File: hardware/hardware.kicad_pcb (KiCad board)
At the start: 2 copper layers, 41 parts, among them J2 Conn_01x03, U1 CH32M007G8R6

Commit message: add shunt A- + led + ntc
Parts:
- added Q10: AOD514, AOD514:TRANS_AOD514, F.Cu at (88.4, 31.7)
- added Q11: AOD514, AOD514:TRANS_AOD514, F.Cu at (97.2, 31.7)
- added Q12: AOD514, AOD514:TRANS_AOD514, F.Cu at (106.1, 31.7)
- added Q7: AOD514, AOD514:TRANS_AOD514, F.Cu at (61.8, 31.7)
- added Q8: AOD514, AOD514:TRANS_AOD514, F.Cu at (70.6, 31.7)
- added Q9: AOD514, AOD514:TRANS_AOD514, F.Cu at (79.5, 31.7)
- moved C11 13.8 mm to (116.0, 50.3)

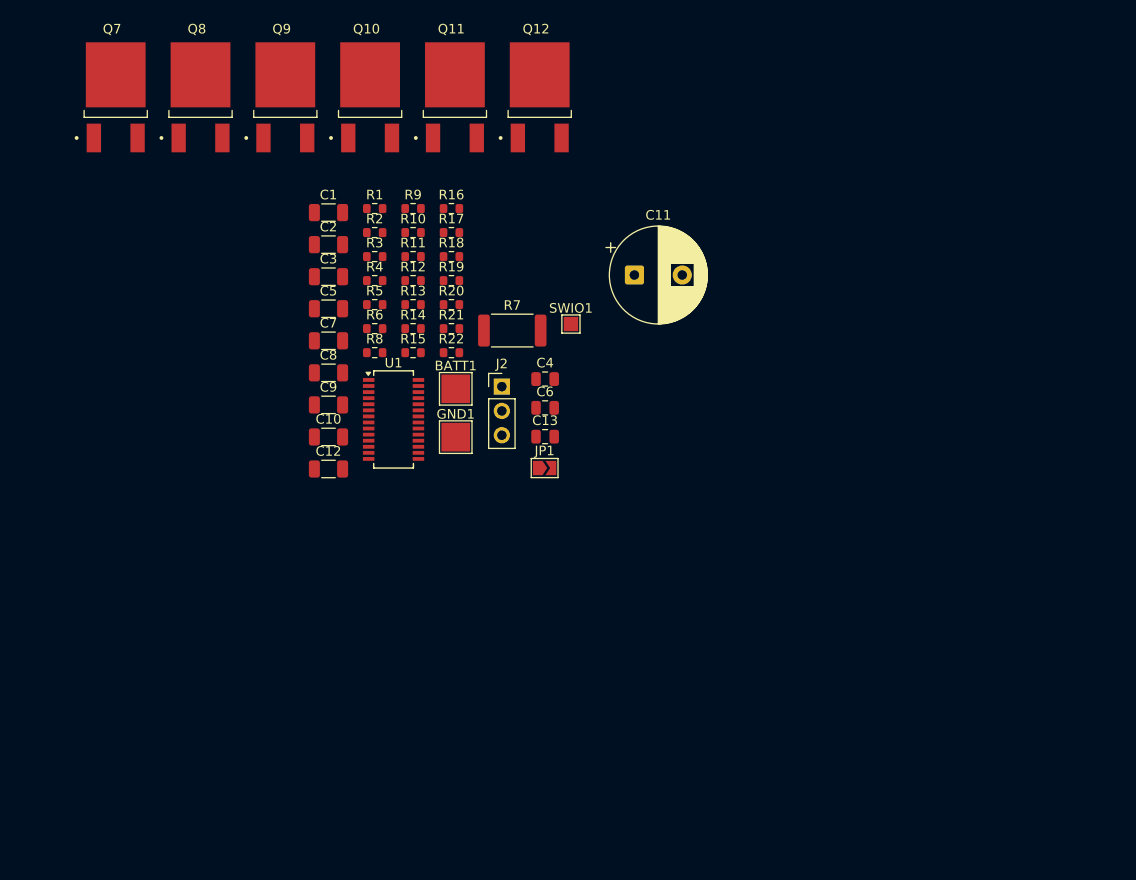
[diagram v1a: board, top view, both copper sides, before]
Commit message: first pcb position
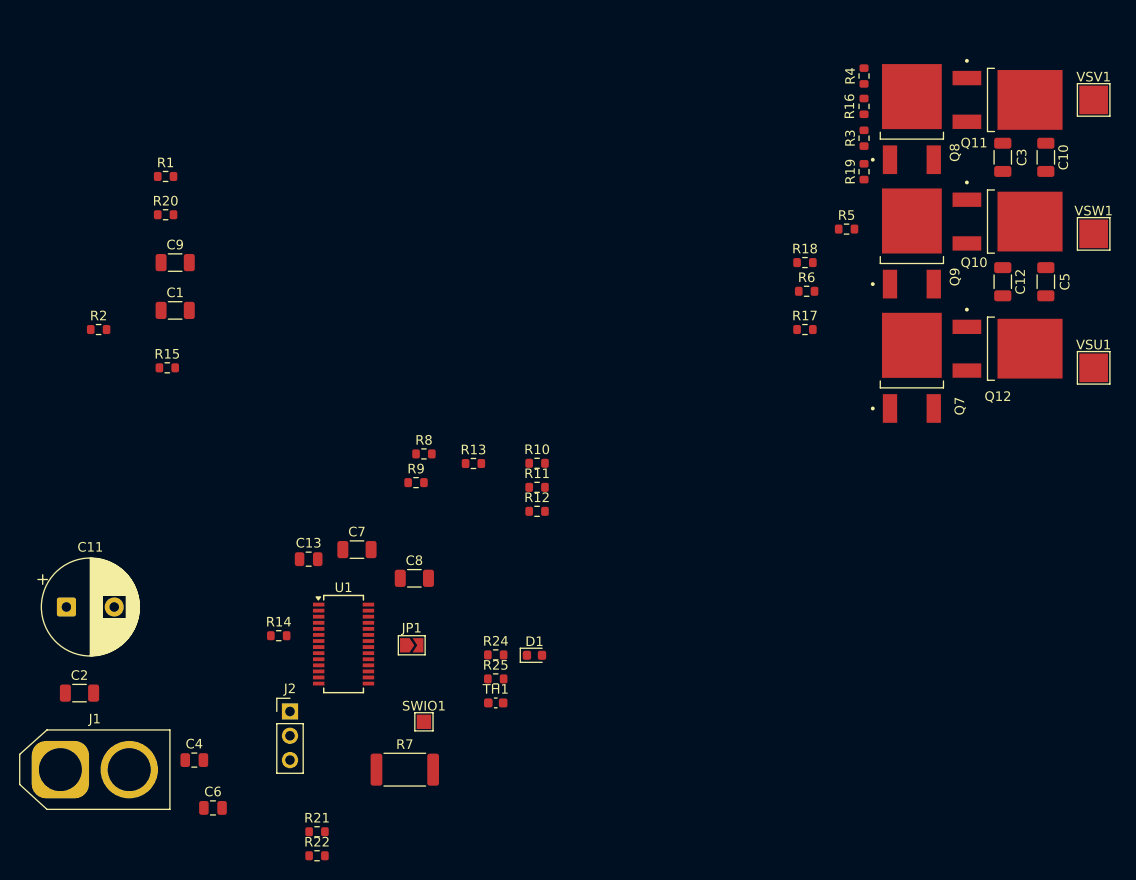
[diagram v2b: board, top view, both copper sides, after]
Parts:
- removed BATT1, GND1: TestPoint_Alt, TestPoint:TestPoint_Pad_3.0x3.0mm
- added D1: BLUE, LED_SMD:LED_0603_1608Metric, F.Cu at (105.6, 90.0)
- added J1: AMASS, Connector_AMASS:AMASS_XT60-F_1x02_P7.20mm_Vertical, F.Cu at (56.0, 102.0)
- added R24: 10k, Resistor_SMD:R_0603_1608Metric, F.Cu at (101.5, 90.0)
- added R25: 1.1k, Resistor_SMD:R_0603_1608Metric, F.Cu at (101.5, 92.5)
- added TH1: NTC 10k B3950, Capacitor_SMD:C_0603_1608Metric, F.Cu at (101.5, 95.0)
- added VSU1: TestPoint_Alt, TestPoint:TestPoint_Pad_3.0x3.0mm, F.Cu at (164.0, 60.0)
- added VSV1: TestPoint_Alt, TestPoint:TestPoint_Pad_3.0x3.0mm, F.Cu at (164.0, 32.0)
- added VSW1: TestPoint_Alt, TestPoint:TestPoint_Pad_3.0x3.0mm, F.Cu at (164.0, 46.0)
- C2: value 100u -> 100n
- R11, R12, R13, R22: value 5.1k -> 8,2k
- moved Q7 87.9 mm to (145.0, 60.0)
- moved C10 80.5 mm to (159.0, 38.0), turned to -90 degrees
- moved C5 75.0 mm to (159.0, 51.0), turned to 90 degrees
- moved Q8 74.4 mm to (145.0, 34.0)
- moved C12 73.1 mm to (154.5, 51.0), turned to -90 degrees
- moved C3 71.6 mm to (154.5, 38.0), turned to 90 degrees
- moved C11 68.8 mm to (56.6, 85.0)
- moved Q10 67.9 mm to (155.0, 44.7), turned to -90 degrees
- moved Q9 67.2 mm to (145.0, 47.0)
- moved Q11 57.8 mm to (155.0, 32.0), turned to -90 degrees
- moved Q12 55.5 mm to (155.0, 58.0), turned to -90 degrees
- moved R4 55.4 mm to (140.0, 29.5), turned to 90 degrees
- moved R22 54.4 mm to (82.8, 111.0)
- moved R21 54.4 mm to (82.8, 108.5)
- moved C6 54.3 mm to (72.0, 106.0)
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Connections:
- C11 pad 2: GND -> A-
- C13 pad 2: GND -> A-
- C2 pad 2: GND -> A-
- C4 pad 2: GND -> A-
- C6 pad 2: GND -> A-
- C7 pad 1: GND -> A-
- C8 pad 1: GND -> A-
- J2 pad 2: GND -> A-
- R11 pad 2: GND -> A-
- R12 pad 2: GND -> A-
- R13 pad 2: GND -> A-
- R15 pad 2: GND -> A-
- R16 pad 2: GND -> A-
- R17 pad 2: GND -> A-
- R22 pad 2: GND -> A-
- R7 pad 2: GND -> A-
- U1 pad 25: GND -> A-
- U1 pad 26: unconnected-(U1-PC4/SDA/A2-Pad26) -> LED
- U1 pad 28: unconnected-(U1-PA4/ON2/A--Pad28) -> A-
- U1 pad 6: unconnected-(U1-PD6/A6-Pad6) -> NTC

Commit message: fix mosfet postion
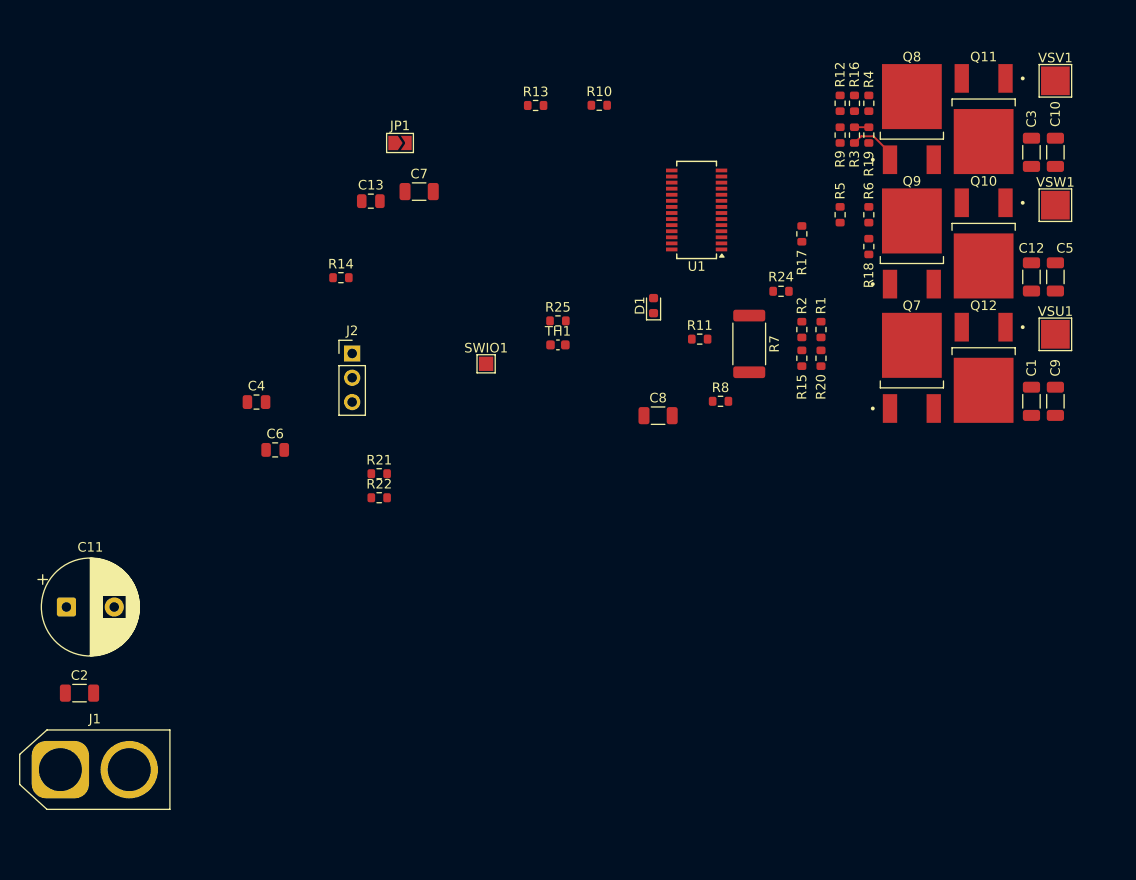
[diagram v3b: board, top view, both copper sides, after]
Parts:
- moved C9 93.1 mm to (160.0, 63.5), turned to -90 degrees
- moved C1 90.0 mm to (157.5, 63.5), turned to 90 degrees
- moved R2 73.5 mm to (133.5, 56.0), turned to 90 degrees
- moved R1 70.3 mm to (135.5, 56.0), turned to 90 degrees
- moved R20 70.1 mm to (135.5, 59.0), turned to 90 degrees
- moved R15 66.3 mm to (133.5, 59.0), turned to -90 degrees
- moved U1 58.5 mm to (122.5, 43.5), turned to 180 degrees
- moved R9 57.3 mm to (137.5, 35.7), turned to 90 degrees
- moved R7 57.2 mm to (128.0, 57.5), turned to -90 degrees
- moved R12 53.1 mm to (137.5, 32.4), turned to 90 degrees
- moved JP1 52.5 mm to (91.5, 36.5)
- moved R24 48.3 mm to (131.3, 52.0), turned to 180 degrees
- moved D1 38.6 mm to (118.0, 53.5), turned to 90 degrees
- moved TH1 38.0 mm to (108.0, 57.6)
- moved C13 38.0 mm to (88.5, 42.6)
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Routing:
- net Net-(Q8-Pad1): track 0.00 -> 5.44 mm
- net HGV: track 0.00 -> 1.50 mm
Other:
- copper layers 2 -> 4

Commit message: finish pcb wiring + change batt+ capacitors
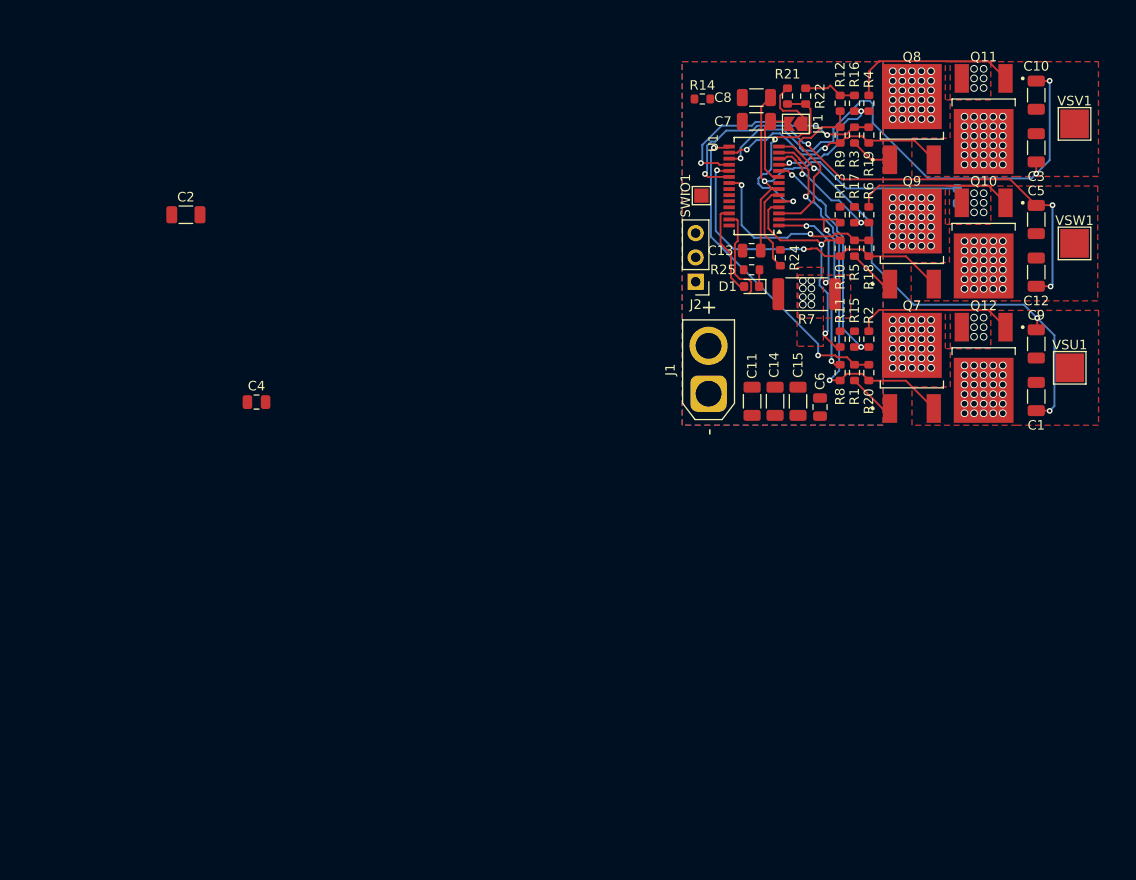
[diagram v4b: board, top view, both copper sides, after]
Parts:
- added C14: 100n, Capacitor_SMD:C_1206_3216Metric, F.Cu at (130.7, 63.5)
- added C15: 100n, Capacitor_SMD:C_1206_3216Metric, F.Cu at (133.1, 63.5)
- C11: value 470µF -> 100n; footprint Capacitor_THT:CP_Radial_D10.0mm_P5.00mm -> Capacitor_SMD:C_1206_3216Metric
- J1: footprint Connector_AMASS:AMASS_XT60-F_1x02_P7.20mm_Vertical -> Connector_AMASS:AMASS_XT30U-F_1x02_P5.0mm_Vertical
- TH1: moved to B.Cu
- moved J1 78.3 mm to (123.8, 62.7), turned to 90 degrees
- moved C11 74.8 mm to (128.3, 63.5), turned to -90 degrees
- moved R22 61.2 mm to (133.9, 31.6), turned to 90 degrees
- moved R21 58.1 mm to (132.0, 31.6), turned to -90 degrees
- moved C6 57.1 mm to (135.4, 64.1), turned to -90 degrees
- moved C2 51.2 mm to (69.1, 44.0)
- moved TH1 44.6 mm to (149.8, 42.0), turned to -90 degrees
- moved R14 42.1 mm to (123.1, 31.9)
- moved JP1 41.4 mm to (132.9, 34.5), turned to 180 degrees
- moved C13 40.1 mm to (128.2, 47.8), turned to 180 degrees
- moved J2 36.7 mm to (122.4, 51.0), turned to 180 degrees
- moved C7 36.0 mm to (128.8, 34.2)
- moved C8 34.8 mm to (128.8, 31.8)
- moved R13 33.8 mm to (137.5, 44.0), turned to 90 degrees
- moved R10 29.3 mm to (137.5, 47.5), turned to 90 degrees
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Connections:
- C11 pad 2: A- -> GND
- C13 pad 2: A- -> GND
- C2 pad 2: A- -> GND
- C4 pad 2: A- -> GND
- C6 pad 2: A- -> GND
- C7 pad 1: A- -> GND
- C8 pad 1: A- -> GND
- J1 pad 1: A- -> GND
- J2 pad 2: A- -> GND
- R11 pad 2: A- -> GND
- R12 pad 2: A- -> GND
- R13 pad 2: A- -> GND
- R15 pad 2: A- -> GND
- R16 pad 2: A- -> GND
- R17 pad 2: A- -> GND
- R22 pad 2: A- -> GND
- R24 pad 2: A- -> GND
- R25 pad 2: A- -> GND
- R7 pad 2: A- -> GND
- U1 pad 25: A- -> GND
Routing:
- net BSTW: track 0.00 -> 56.3 mm, vias 0 -> 4
- net BSTV: track 0.00 -> 55.6 mm, vias 0 -> 3
- net BSTU: track 0.00 -> 50.2 mm, vias 0 -> 3
- net +5V: track 0.00 -> 40.9 mm, vias 0 -> 1
- net VSU: track 0.00 -> 40.8 mm, vias 0 -> 32
- net HGU: track 0.00 -> 33.8 mm, vias 0 -> 2
- net VSW: track 0.00 -> 33.4 mm, vias 0 -> 32
- net VSV: track 0.00 -> 25.2 mm, vias 0 -> 32
- net LGU: track 0.00 -> 24.2 mm, vias 0 -> 2
- net PD4: track 0.00 -> 23.7 mm, vias 0 -> 2
- net PD2: track 0.00 -> 23.3 mm, vias 0 -> 2
- net HGV: track 1.50 -> 24.3 mm, vias 0 -> 2
- net BATT_VOLT: track 0.00 -> 20.6 mm, vias 0 -> 2
- net HGW: track 0.00 -> 20.1 mm, vias 0 -> 2
- net PD3: track 0.00 -> 18.1 mm
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- added copper zone on In1.Cu, net +BATT
- added copper zone on B.Cu, net GND
- added copper zone on F.Cu, net GND
- added copper zone on F.Cu, net OP1
- added copper zone on In2.Cu, net OP1
- added copper zone on F.Cu, net VSU
- added copper zone on In1.Cu, net VSU
- added copper zone on F.Cu, net VSV
- added copper zone on In1.Cu, net VSV
- added copper zone on F.Cu, net VSW
- added copper zone on In1.Cu, net VSW

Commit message: add revision + finish PCB
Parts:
- moved C2 62.8 mm to (130.6, 56.9), turned to 90 degrees
- moved C4 52.1 mm to (128.2, 56.9), turned to 90 degrees
- moved R14 2.60 mm to (124.1, 34.3)
- moved C6 1.20 mm to (135.4, 62.9)
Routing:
- net NTC: track 9.13 -> 33.2 mm, vias 0 -> 1
- net +5V: track 40.9 -> 58.9 mm
- net +BATT: track 5.89 -> 22.4 mm, vias 90 -> 91
- net PA1: track 0.00 -> 5.27 mm
- net Net-(U1-PC5/RST/T2C1/SCL/CP0): track 10.0 -> 13.7 mm
- net GND: track 5.82 -> 9.15 mm, vias 0 -> 38
- net SWIO: track 0.00 -> 2.92 mm
- net HGV: track 24.3 -> 26.7 mm
- net BSTU: track 50.2 -> 52.5 mm
- net VSU: track 40.8 -> 39.5 mm
- net HGU: track 33.8 -> 32.9 mm
- net VSW: track 33.4 -> 32.7 mm
- net LED: track 9.76 -> 10.4 mm
- net BSTV: track 55.6 -> 55.0 mm
- added copper zone on F.Cu, net +BATT
- added copper zone on B.Cu, net VSU
- added copper zone on B.Cu, net VSV
- added copper zone on B.Cu, net VSW
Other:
- board outline added: 45 x 40 mm
